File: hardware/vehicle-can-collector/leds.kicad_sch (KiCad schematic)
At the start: 27 parts, among them U1101 TCA9534

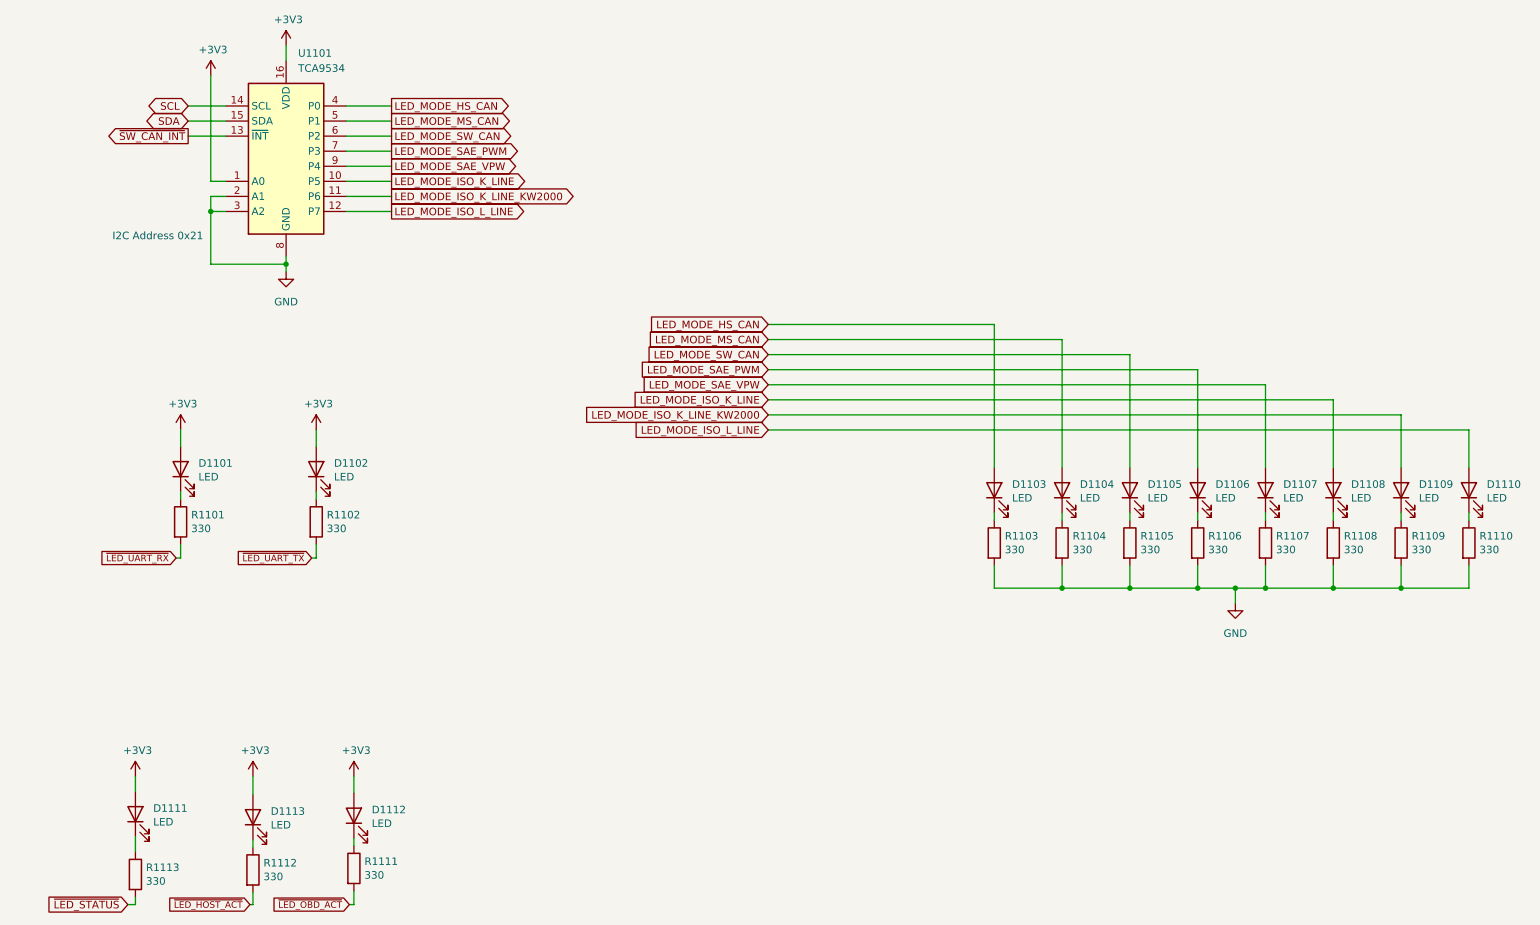
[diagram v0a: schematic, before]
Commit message: Added footprints, tossed all footprints onto PCB
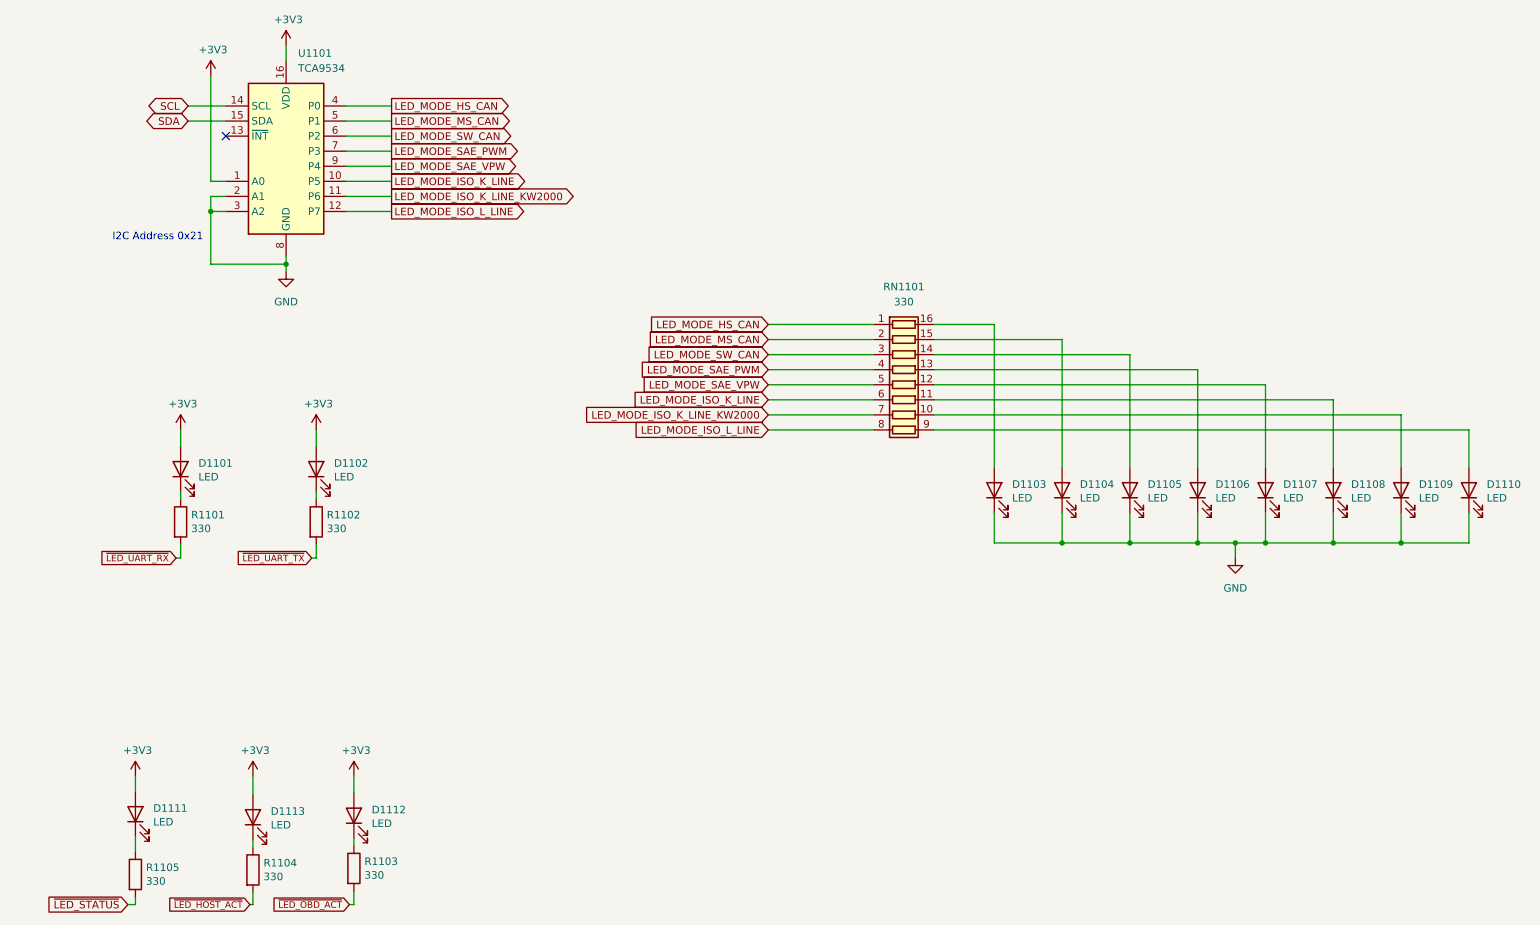
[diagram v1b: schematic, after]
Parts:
- removed R1103, R1104, R1105, R1106, R1107, R1108, R1109, R1110: 330, symbol Device:R
- added RN1101: 330, Resistor_SMD:R_Array_Convex_8x0602, symbol Device:R_Pack08
- D1101, D1102, D1103, D1104, D1105, D1106, D1107, D1108, D1109, D1110, D1111, D1112, D1113: footprint (none) -> LED_SMD:LED_0805_2012Metric_Pad1.15x1.40mm_HandSolder
- R1101, R1102: footprint (none) -> Resistor_SMD:R_0805_2012Metric_Pad1.20x1.40mm_HandSolder
- R1103: renamed from R1111; footprint (none) -> Resistor_SMD:R_0805_2012Metric_Pad1.20x1.40mm_HandSolder
- R1104: renamed from R1112; footprint (none) -> Resistor_SMD:R_0805_2012Metric_Pad1.20x1.40mm_HandSolder
- R1105: renamed from R1113; footprint (none) -> Resistor_SMD:R_0805_2012Metric_Pad1.20x1.40mm_HandSolder
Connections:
- net GND: now also D1103.1 (K), D1104.1 (K), D1105.1 (K), D1106.1 (K), D1107.1 (K), D1108.1 (K), D1109.1 (K), D1110.1 (K)
- net LED_MODE_HS_CAN: now also RN1101.1 (R1.1); no longer D1103.2 (A)
- net LED_MODE_ISO_K_LINE: now also RN1101.6 (R6.1); no longer D1108.2 (A)
- net LED_MODE_ISO_K_LINE_KW2000: now also RN1101.7 (R7.1); no longer D1109.2 (A)
- net LED_MODE_ISO_L_LINE: now also RN1101.8 (R8.1); no longer D1110.2 (A)
- net LED_MODE_MS_CAN: now also RN1101.2 (R2.1); no longer D1104.2 (A)
- net LED_MODE_SAE_PWM: now also RN1101.4 (R4.1); no longer D1106.2 (A)
- net LED_MODE_SAE_VPW: now also RN1101.5 (R5.1); no longer D1107.2 (A)
- net LED_MODE_SW_CAN: now also RN1101.3 (R3.1); no longer D1105.2 (A)
- net ~{SW_CAN_INT}: no longer names the net of U1101.13 (~{INT})
- new net: D1110.2 (A), RN1101.9 (R8.2)
- new net: D1108.2 (A), RN1101.11 (R6.2)
- new net: D1105.2 (A), RN1101.14 (R3.2)
- new net: D1109.2 (A), RN1101.10 (R7.2)
- new net: D1107.2 (A), RN1101.12 (R5.2)
- new net: D1106.2 (A), RN1101.13 (R4.2)
- new net: D1104.2 (A), RN1101.15 (R2.2)
- new net: D1103.2 (A), RN1101.16 (R1.2)
- no-connect marks 0 -> 1
